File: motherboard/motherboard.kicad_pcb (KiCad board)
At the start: 2 copper layers, 79.8 x 53.3 mm, 41 parts, among them J1 locked, J2 PROGRAM, J3 Battery / Pitot/ Orientation, J4 c02 censor, J5 shaftencorder, J6 USB_C_Receptacle_USB2.0, J7 SparLoad, J8 lidar, J9 Control Board, Q1 2N7002K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

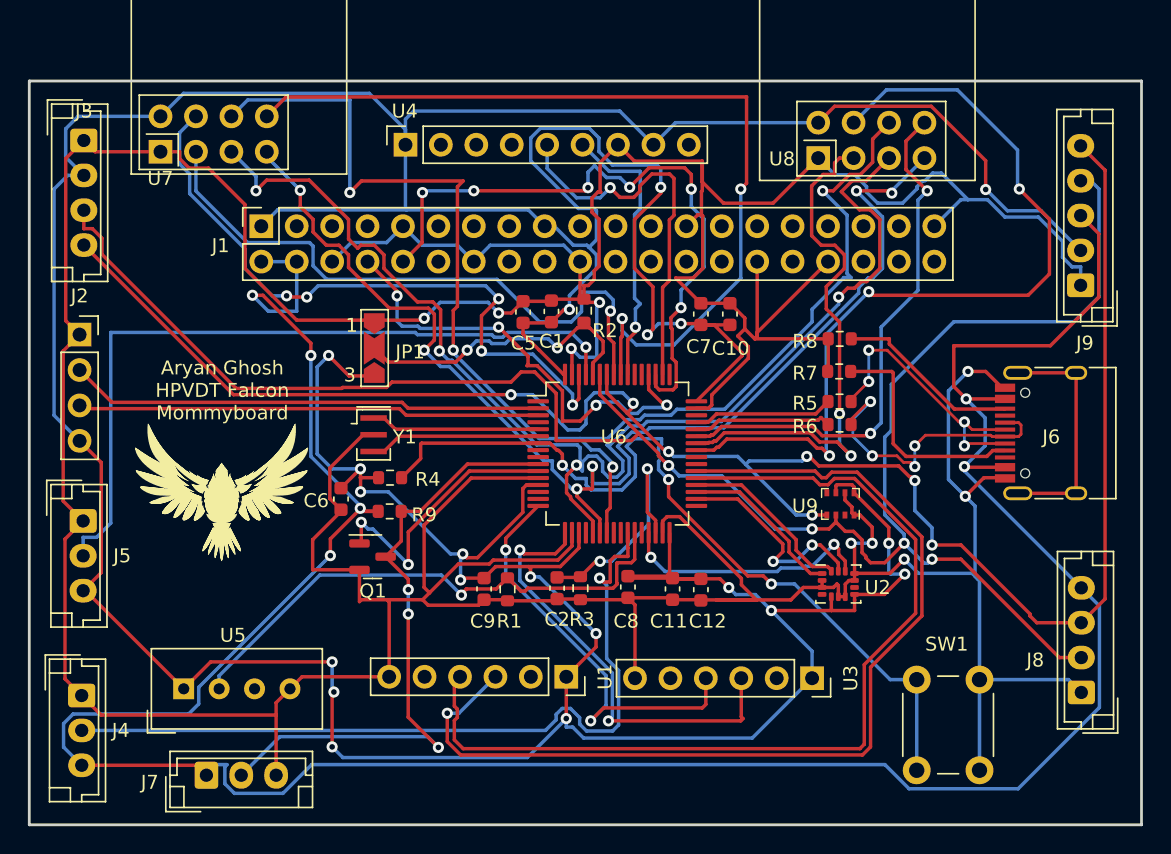
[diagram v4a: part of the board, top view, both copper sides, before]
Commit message: Completed feedback for draft 1 round 1
addded thicker traces, disconnected 3.3V from RPi, changed capacitor location, added mounting holes for RPi, added mounting holes to the board, added programming labels
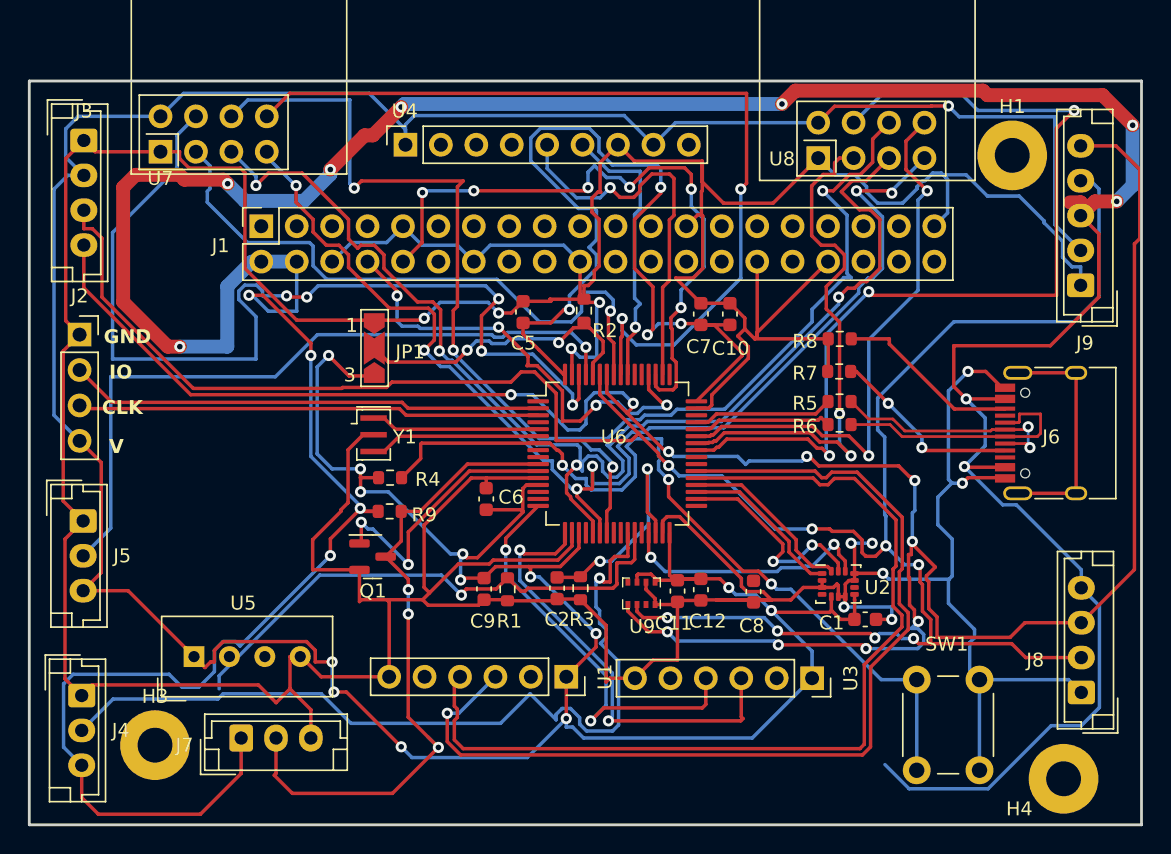
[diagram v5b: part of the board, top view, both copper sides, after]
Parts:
- added H1: MountingHole, MountingHole:MountingHole_2.5mm_Pad, F.Cu at (142.6, 66.3)
- added H3: MountingHole, MountingHole:MountingHole_2.5mm_Pad, F.Cu at (81.2, 108.6)
- added H4: MountingHole, MountingHole:MountingHole_2.5mm_Pad, F.Cu at (146.3, 111.0)
- moved C1 31.5 mm to (132.1, 99.6), turned to 0 degrees
- moved U9 15.6 mm to (116.0, 97.7)
- moved C6 10.4 mm to (104.9, 90.9), turned to -90 degrees
- moved C8 9.01 mm to (124.1, 97.6)
- moved J7 3.65 mm to (87.3, 108.1)
- moved U5 2.43 mm to (83.9, 102.2)
- moved C11 0.39 mm to (118.6, 97.5)
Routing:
- net +5V: track 198.7 -> 273.0 mm, vias 6 -> 13
- net +3.3V: track 395.9 -> 352.9 mm, vias 20 -> 18
- net /I2C_{SCK}: track 135.8 -> 171.2 mm, vias 7 -> 10
- net /I2C_{SDA}: track 137.0 -> 162.7 mm, vias 4 -> 8
- net /TELE_{CS}-int: track 48.4 -> 70.9 mm
- net GND: track 431.9 -> 446.0 mm, vias 9 -> 11
- net /TELE_{CS}-E: track 61.5 -> 68.2 mm
- net /D-: track 21.0 -> 17.1 mm, vias 4 -> 2
- net /CO_{2}: track 57.1 -> 61.0 mm
- net /D+: track 22.1 -> 18.6 mm, vias 4 -> 0
- net Net-(J6-CC1): track 16.7 -> 13.9 mm, vias 0 -> 2
- net /SHAFTENC: track 54.2 -> 51.6 mm
- net /TELE_{IRQ}-E: track 38.3 -> 40.3 mm
- net /OneWire_{RX}: track 45.8 -> 47.7 mm
- net /USART6_{RX}: track 72.6 -> 72.0 mm
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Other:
- board text added: "CLK"
- board text added: "GND"
- board text added: "IO"
- board text added: "V"

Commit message: Minor tweaks to motherboard
- Changed DRC settings to allow tighter copper spacing.
- Removed RPi 3.3V connection
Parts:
- added H2: MountingHole, MountingHole:MountingHole_2.5mm_Pad, F.Cu at (83.0, 122.5)
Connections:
- J1 pad 1: +3.3V -> unconnected-(J1-3V3-Pad1)
- J1 pad 17: +3.3V -> unconnected-(J1-3V3-Pad17)
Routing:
- net unconnected-(J1-3V3-Pad17): track 0.00 -> 0.69 mm
- net +3.3V: track 352.9 -> 352.2 mm
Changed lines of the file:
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@@
   (net 102 "unconnected-(U9-CSB-Pad2)")
   (net 103 "unconnected-(U9-SDO-Pad5)")
+  (net 104 "unconnected-(J1-3V3-Pad1)")
+  (net 105 "unconnected-(J1-3V3-Pad17)")
   (footprint "Package_LGA:LGA-14_3x2.5mm_P0.5mm_LayoutBorder3x4y" (layer "F.Cu")
     (at 130.1496 97.028)
@@
       (stroke (width 0.12) (type default)) (fill none) (layer "F.Fab"))
     (pad "1" thru_hole rect locked (at 0 0 90) (size 1.7 1.7) (drill 1) (layers "*.Cu" "*.Mask")
-      (net 1 "+3.3V") (pinfunction "3V3") (pintype "power_in"))
+      (net 104 "unconnected-(J1-3V3-Pad1)") (pinfunction "3V3") (pintype "power_in+no_connect"))
     (pad "2" thru_hole oval locked (at -2.54 0 90) (size 1.7 1.7) (drill 1) (layers "*.Cu" "*.Mask")
       (net 4 "+5V") (pinfunction "5V") (pintype "power_in"))
@@
       (net 14 "unconnected-(J1-GPIO23-Pad16)") (pinfunction "GPIO23") (pintype "bidirectional+no_connect"))
     (pad "17" thru_hole oval locked (at 0 20.32 90) (size 1.7 1.7) (drill 1) (layers "*.Cu" "*.Mask")
-      (net 1 "+3.3V") (pinfunction "3V3") (pintype "power_in"))
+      (net 105 "unconnected-(J1-3V3-Pad17)") (pinfunction "3V3") (pintype "power_in+no_connect"))
     (pad "18" thru_hole oval locked (at -2.54 20.32 90) (size 1.7 1.7) (drill 1) (layers "*.Cu" "*.Mask")
       (net 15 "unconnected-(J1-GPIO24-Pad18)") (pinfunction "GPIO24") (pintype "bidirectional+no_connect"))
@@
     )
   )
+  (footprint "MountingHole:MountingHole_2.5mm_Pad" (layer "F.Cu")
+    (at 82.95 122.5)
+    (descr "Mounting Hole 2.5mm")
+    (tags "mounting hole 2.5mm")
+    (property "Sheetfile" "motherboard.kicad_sch")
+    (property "Sheetname" "")
+    (property "ki_description" "Mounting Hole without connection")
+    (property "ki_keywords" "mounting hole")
+    (attr exclude_from_pos_files)
+    (fp_text reference "H2" (at 0 -3.5) (layer "F.SilkS")
+        (effects (font (size 1 1) (thickness 0.15)))
+    )
+    (fp_text value "MountingHole" (at 0 3.5) (layer "F.Fab")
+        (effects (font (size 1 1) (thickness 0.15)))
+    )
+    (fp_text user "${REFERENCE}" (at 0 0) (layer "F.Fab")
+        (effects (font (size 1 1) (thickness 0.15)))
+    )
+    (fp_circle (center 0 0) (end 2.5 0)
+      (stroke (width 0.15) (type solid)) (fill none) (layer "Cmts.User"))
+    (fp_circle (center 0 0) (end 2.75 0)
+      (stroke (width 0.05) (type solid)) (fill none) (layer "F.CrtYd"))
+    (pad "1" thru_hole circle (at 0 0) (size 5 5) (drill 2.5) (layers "*.Cu" "*.Mask"))
+  )
   (footprint "Resistor_SMD:R_0603_1608Metric" (layer "F.Cu")
     (at 130.239 85.598)
@@
   (segment (start 93.853 104.648) (end 93.98 104.775) (width 0.25) (layer "B.Cu") (net 1))
   (segment (start 116.8908 65.532) (end 118.47345 63.94935) (width 0.25) (layer "B.Cu") (net 1))
-  (segment (start 109.781299 71.374) (end 109.093 71.374) (width 0.25) (layer "B.Cu") (net 1))
   (segment (start 93.854396 88.773) (end 95.885 88.773) (width 0.25) (layer "B.Cu") (net 1))
   (segment (start 125.349 98.933) (end 124.206 97.79) (width 0.25) (layer "B.Cu") (net 1))
@@
   (segment (start 90.5885 76.366603) (end 88.863 76.366603) (width 0.25) (layer "B.Cu") (net 101))
   (segment (start 108.2355 80.5495) (end 111.091219 83.405219) (width 0.25) (layer "B.Cu") (net 101))
+  (segment (start 109.781299 71.374) (end 109.093 71.374) (width 0.25) (layer "B.Cu") (net 105))
 )

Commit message: Edited layout
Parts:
- added H5: MountingHole, MountingHole:MountingHole_2.7mm_M2.5, F.Cu at (141.9, 95.8)
- added H6: MountingHole, MountingHole:MountingHole_2.7mm_M2.5, F.Cu at (141.9, 72.8)
- added H7: MountingHole, MountingHole:MountingHole_2.7mm_M2.5, F.Cu at (83.9, 72.8)
- added H8: MountingHole, MountingHole:MountingHole_2.7mm_M2.5, F.Cu at (83.9, 95.8)
- moved J1 25.5 mm to (114.2, 70.2)
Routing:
- net GND: track 446.0 -> 499.8 mm, vias 11 -> 12
- net +5V: track 273.0 -> 297.7 mm
- net /SPI1MOSI: track 95.5 -> 94.3 mm
- net /OneWire_{RX}: track 47.7 -> 46.6 mm
- net /TELE_{CE}-E: track 38.6 -> 39.4 mm

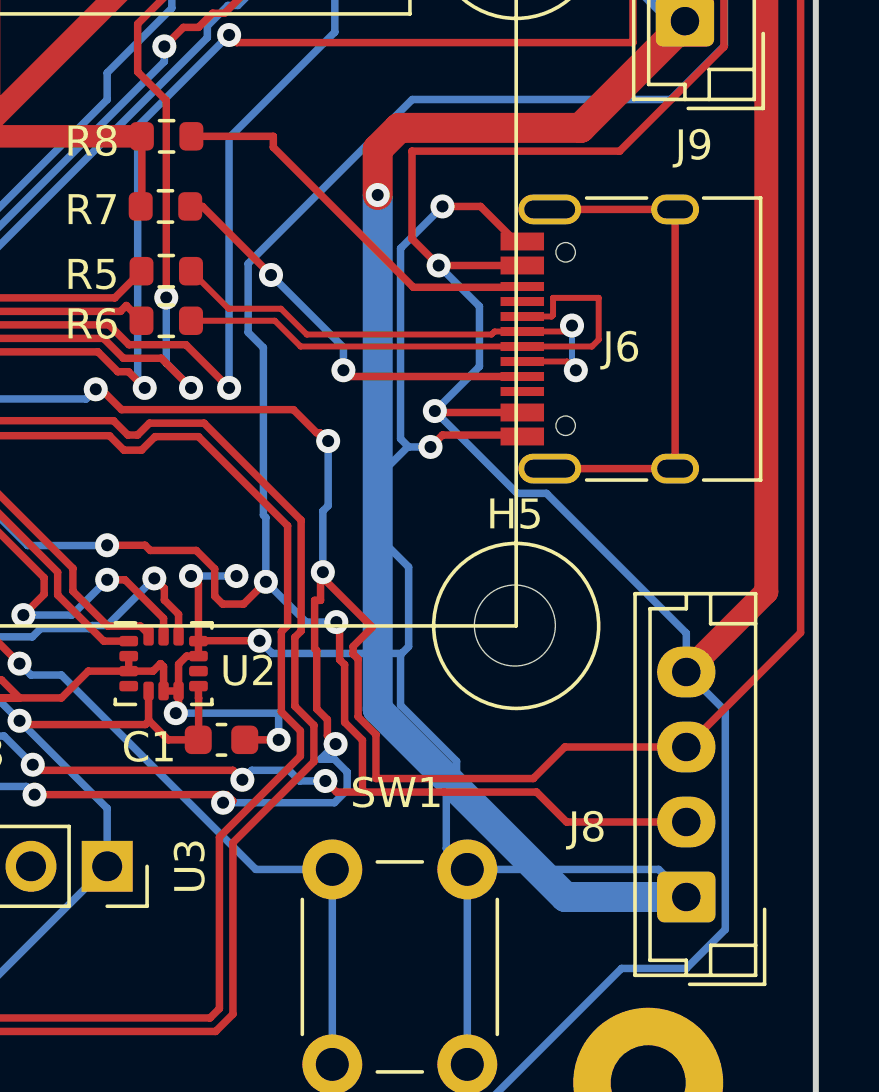
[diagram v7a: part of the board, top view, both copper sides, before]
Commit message: Edited rev2 layout
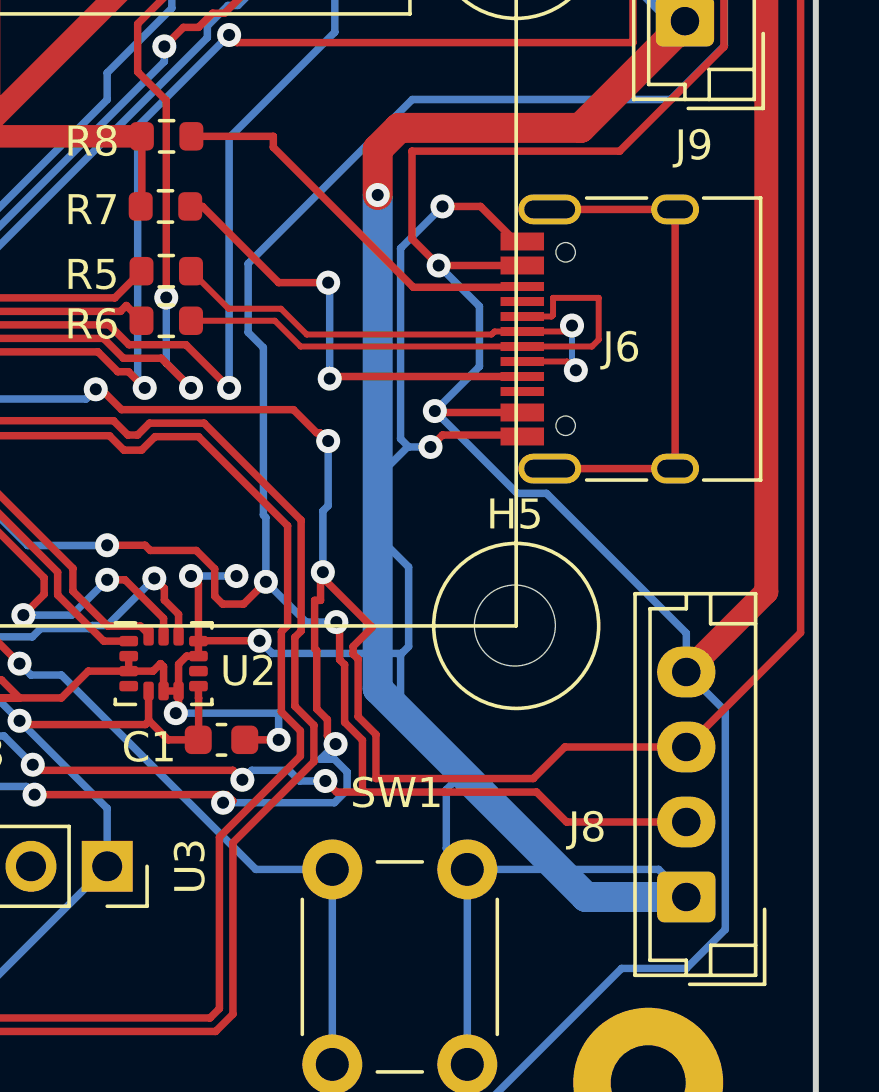
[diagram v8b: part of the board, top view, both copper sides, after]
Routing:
- net Net-(J6-CC1): track 13.9 -> 15.3 mm
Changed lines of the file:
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@@
   (segment (start 110.47 72.751) (end 111.633 73.914) (width 0.5) (layer "B.Cu") (net 2))
   (segment (start 134.885 68.815634) (end 135.861284 67.83935) (width 0.7) (layer "B.Cu") (net 2))
+  (segment (start 137.287 97.8662) (end 144.2282 104.8074) (width 1) (layer "B.Cu") (net 2))
   (segment (start 137.033 71.374) (end 137.9855 70.4215) (width 1) (layer "B.Cu") (net 2))
   (segment (start 138.303 89.789) (end 138.32 89.806) (width 0.25) (layer "B.Cu") (net 2))
@@
   (segment (start 133.085 69.371293) (end 133.612207 69.8985) (width 0.7) (layer "B.Cu") (net 2))
   (segment (start 93.7768 72.751) (end 98.9584 72.751) (width 0.5) (layer "B.Cu") (net 2))
+  (segment (start 144.2282 104.8074) (end 147.574 104.8074) (width 1) (layer "B.Cu") (net 2))
   (segment (start 137.9855 68.0085) (end 137.8585 67.8815) (width 1) (layer "B.Cu") (net 2))
   (segment (start 138.049 89.535) (end 138.303 89.789) (width 0.25) (layer "B.Cu") (net 2))
@@
   (segment (start 138.684 67.691) (end 137.668 67.691) (width 1) (layer "B.Cu") (net 2))
   (segment (start 138.089551 96.687551) (end 138.049 96.728102) (width 0.25) (layer "B.Cu") (net 2))
-  (segment (start 137.287 81.407) (end 137.287 98.552) (width 1) (layer "B.Cu") (net 2))
   (segment (start 112.8255 80.772) (end 111.633 80.772) (width 0.25) (layer "B.Cu") (net 2))
   (segment (start 138.049 96.728102) (end 138.049 98.415695) (width 0.25) (layer "B.Cu") (net 2))
@@
   (segment (start 139.446 81.788) (end 138.049 83.185) (width 0.25) (layer "B.Cu") (net 2))
   (segment (start 111.633 80.772) (end 111.002299 80.141299) (width 0.25) (layer "B.Cu") (net 2))
+  (segment (start 137.287 81.407) (end 137.287 97.8662) (width 1) (layer "B.Cu") (net 2))
   (segment (start 140.2736 110.3872) (end 140.2736 103.8872) (width 0.25) (layer "B.Cu") (net 2))
   (segment (start 130.0574 67.83935) (end 131.806589 67.83935) (width 0.7) (layer "B.Cu") (net 2))
-  (segment (start 137.287 98.552) (end 143.5424 104.8074) (width 1) (layer "B.Cu") (net 2))
   (segment (start 140.437 69.444) (end 138.684 67.691) (width 1) (layer "B.Cu") (net 2))
   (segment (start 133.985 98.679) (end 133.985 99.568) (width 0.25) (layer "B.Cu") (net 2))
@@
   (segment (start 139.917 100.884305) (end 139.573 101.228305) (width 0.25) (layer "B.Cu") (net 2))
   (segment (start 131.806589 67.83935) (end 131.827939 67.818) (width 0.7) (layer "B.Cu") (net 2))
-  (segment (start 143.5424 104.8074) (end 147.574 104.8074) (width 1) (layer "B.Cu") (net 2))
   (segment (start 138.318 93.808604) (end 137.287 92.777604) (width 0.25) (layer "B.Cu") (net 2))
   (segment (start 128.7074 66.48935) (end 130.0574 67.83935) (width 0.7) (layer "B.Cu") (net 2))
@@
   (segment (start 105.305695 79.153) (end 92.795695 79.153) (width 0.25) (layer "B.Cu") (net 38))
   (segment (start 89.779695 82.169) (end 77.978 82.169) (width 0.25) (layer "B.Cu") (net 38))
+  (segment (start 135.7576 87.4576) (end 142.1066 87.4576) (width 0.25) (layer "F.Cu") (net 39))
+  (segment (start 135.6868 87.5284) (end 135.7576 87.4576) (width 0.25) (layer "F.Cu") (net 39))
   (segment (start 131.445 81.788) (end 131.0376 81.788) (width 0.25) (layer "F.Cu") (net 39))
-  (segment (start 136.3526 87.4576) (end 136.144 87.249) (width 0.25) (layer "F.Cu") (net 39))
-  (segment (start 142.1066 87.4576) (end 136.3526 87.4576) (width 0.25) (layer "F.Cu") (net 39))
-  (segment (start 133.731 84.074) (end 131.445 81.788) (width 0.25) (layer "F.Cu") (net 39))
-  (via (at 133.731 84.074) (size 0.8) (drill 0.4) (layers "F.Cu" "B.Cu") (net 39))
-  (via (at 136.144 87.249) (size 0.8) (drill 0.4) (layers "F.Cu" "B.Cu") (net 39))
-  (segment (start 136.144 87.249) (end 136.144 86.487) (width 0.25) (layer "B.Cu") (net 39))
-  (segment (start 136.144 86.487) (end 133.731 84.074) (width 0.25) (layer "B.Cu") (net 39))
+  (segment (start 133.985 84.328) (end 131.445 81.788) (width 0.25) (layer "F.Cu") (net 39))
+  (segment (start 135.636 84.328) (end 133.985 84.328) (width 0.25) (layer "F.Cu") (net 39))
+  (via (at 135.636 84.328) (size 0.8) (drill 0.4) (layers "F.Cu" "B.Cu") (net 39))
+  (via (at 135.6868 87.5284) (size 0.8) (drill 0.4) (layers "F.Cu" "B.Cu") (net 39))
+  (segment (start 135.636 84.328) (end 135.6868 84.3788) (width 0.25) (layer "B.Cu") (net 39))
+  (segment (start 135.6868 84.3788) (end 135.6868 87.5284) (width 0.25) (layer "B.Cu") (net 39))
   (segment (start 144.4284 86.4576) (end 142.1066 86.4576) (width 0.2) (layer "F.Cu") (net 40))
   (segment (start 143.0816 85.4576) (end 143.1316 85.4076) (width 0.2) (layer "F.Cu") (net 40))
